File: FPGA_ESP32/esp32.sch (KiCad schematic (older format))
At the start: 1 part

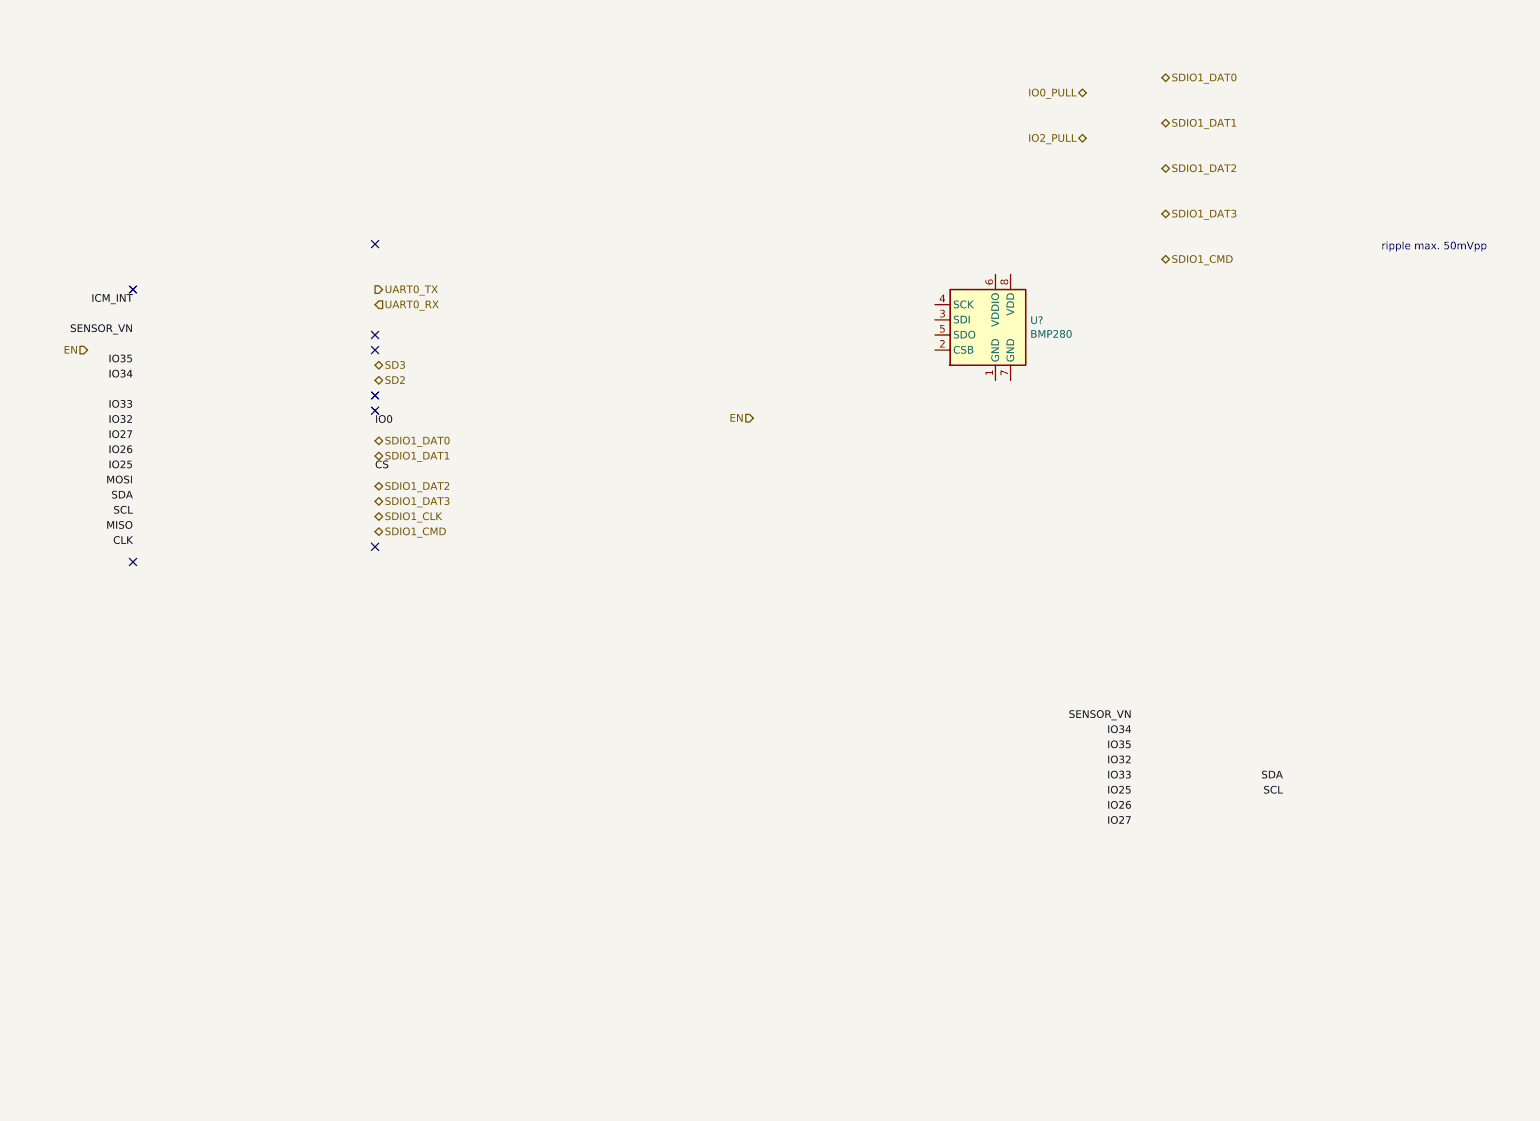
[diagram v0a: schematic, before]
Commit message: FPGA_ESP32 : add header + esp32 with SDIO
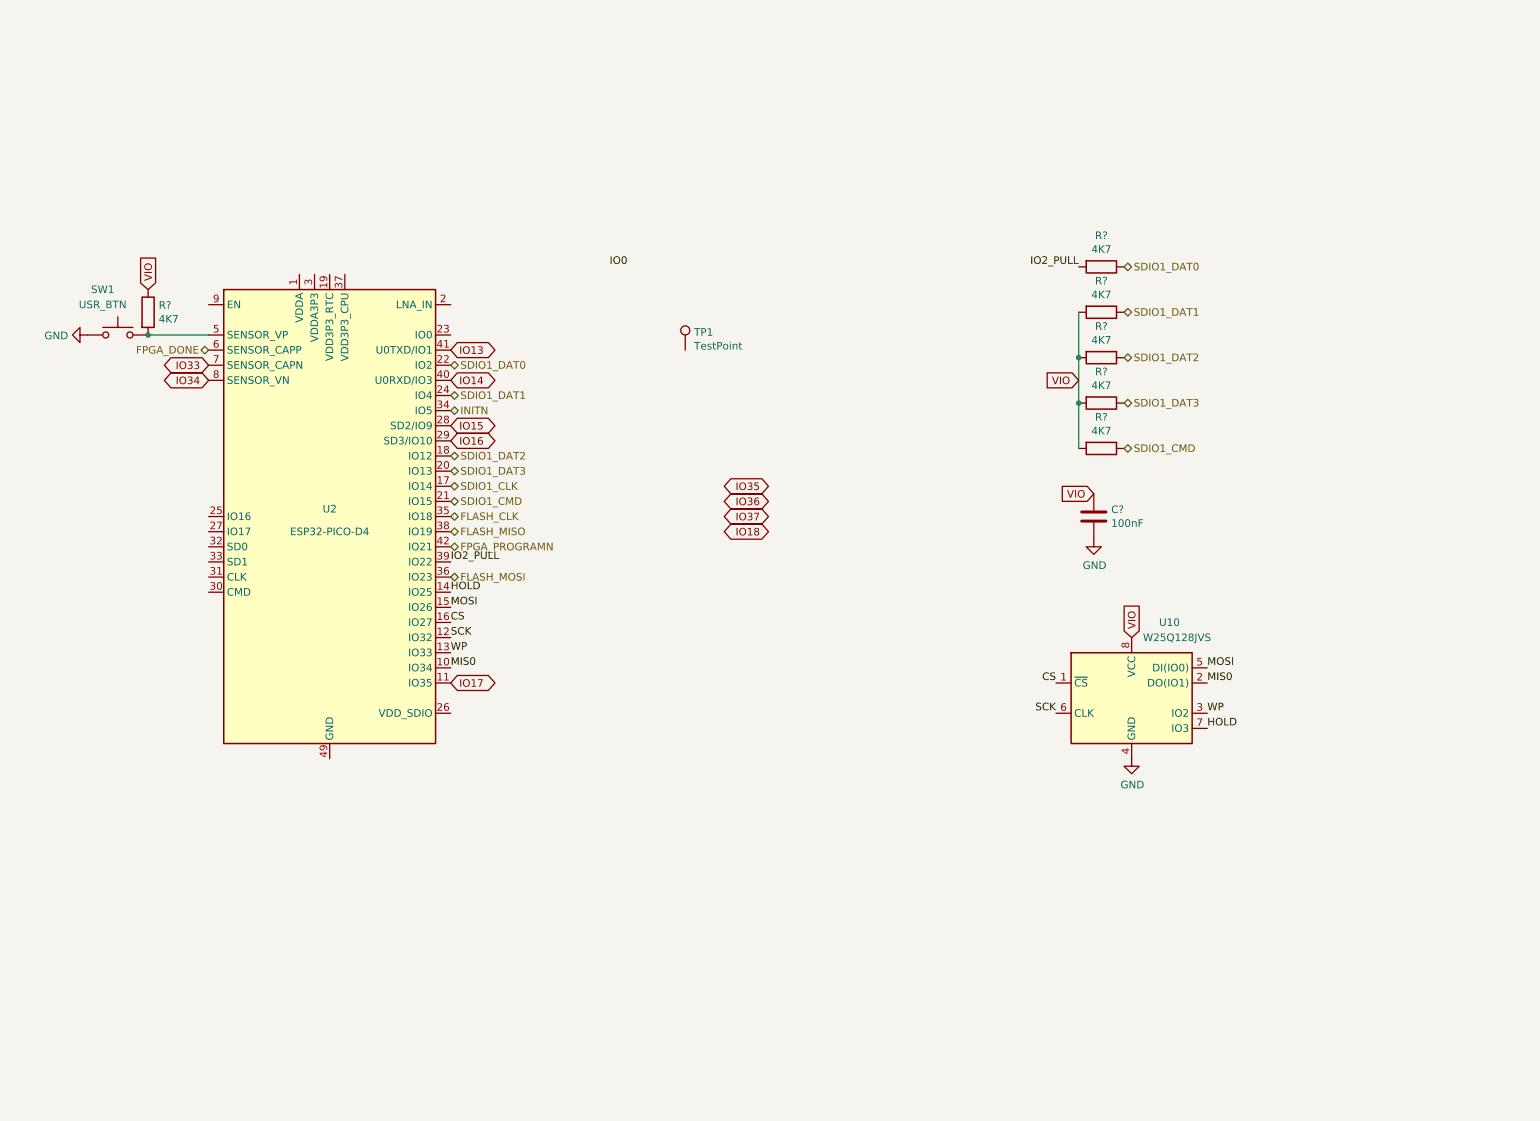
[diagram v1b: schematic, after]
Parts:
- removed U?: BMP280, Package_LGA:Bosch_LGA-8_2x2.5mm_P0.65mm_ClockwisePinNumbering, symbol Sensor_Pressure:BMP280
- added C?: 100nF, symbol Device:C
- added R? (x6): 4K7, symbol Device:R
- added SW1: USR_BTN, Button_Switch_SMD:SW_Push_1P1T_NO_CK_KMR2, symbol Switch:SW_Push
- added TP1: TestPoint, Connector_PinHeader_2.54mm:PinHeader_1x01_P2.54mm_Vertical, symbol Connector:TestPoint
- added U10: W25Q128JVS, Package_SO:SOIC-8_5.23x5.23mm_P1.27mm, symbol Memory_Flash:W25Q128JVS
- added U2: ESP32-PICO-D4, Package_DFN_QFN:QFN-48-1EP_7x7mm_P0.5mm_EP5.3x5.3mm, symbol RF_Module:ESP32-PICO-D4
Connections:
- net CS: now also U10.1 (~CS), U2.16 (IO27)
- net IO2_PULL: now also R?.2, U2.39 (IO22)
- net IO33: now also U2.7 (SENSOR_CAPN)
- net IO34: now also U2.8 (SENSOR_VN)
- net MOSI: now also U10.5 (DI(IO0)), U2.15 (IO26)
- net SDIO1_CLK: now also U2.17 (IO14)
- net SDIO1_CMD: now also R?.1, U2.21 (IO15)
- net SDIO1_DAT0: now also R?.1, U2.22 (IO2)
- net SDIO1_DAT1: now also R?.1, U2.24 (IO4)
- net SDIO1_DAT2: now also R?.1, U2.18 (IO12)
- net SDIO1_DAT3: now also R?.1, U2.20 (IO13)
- new net: R?.2, SW1.2, U2.5 (SENSOR_VP)
- new net: U2.1 (VDDA), U2.43 (VDDA), U2.46 (VDDA)
- new net: U2.3 (VDDA3P3), U2.4 (VDDA3P3)
- new net FLASH_CLK: U2.35 (IO18)
- new net FLASH_MISO: U2.38 (IO19)
- new net FLASH_MOSI: U2.36 (IO23)
- new net FPGA_DONE: U2.6 (SENSOR_CAPP)
- new net FPGA_PROGRAMN: U2.42 (IO21)
- new net GND: C?.1, SW1.1, U10.4 (GND)
- new net HOLD: U10.7 (IO3), U2.14 (IO25)
- new net INITN: U2.34 (IO5)
- new net IO13: U2.41 (U0TXD/IO1)
- new net IO14: U2.40 (U0RXD/IO3)
- new net IO15: U2.28 (SD2/IO9)
- new net IO16: U2.29 (SD3/IO10)
- new net IO17: U2.11 (IO35)
- new net MIS0: U10.2 (DO(IO1)), U2.10 (IO34)
- new net SCK: U10.6 (CLK), U2.12 (IO32)
- new net VIO: C?.2, R?.1, R?.2, R?.2, R?.2, R?.2, U10.8 (VCC)
- new net WP: U10.3 (IO2), U2.13 (IO33)
- no-connect marks 8 -> 0
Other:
- note removed: "ripple max. 50mVpp"

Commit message: FPGA_ESP32 : add 2 psram ic, rf switch
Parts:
- removed R?: 4K7, symbol Device:R
- removed SW1: USR_BTN, Button_Switch_SMD:SW_Push_1P1T_NO_CK_KMR2, symbol Switch:SW_Push
- removed U10: W25Q128JVS, Package_SO:SOIC-8_5.23x5.23mm_P1.27mm, symbol Memory_Flash:W25Q128JVS
- added ANT2: Antenna, TestPoint:TestPoint_Pad_D1.0mm, symbol Connector:TestPoint
- added U10: GD25Q16CEIGR, footprints:PSON50P200X300X50-9N, symbol GD25Q16CEIGR:GD25Q16CEIGR
- added U7: RFX2411, footprints:QFN-20_EP_3x3_Pitch0.4mm, symbol ob:RFX2411
- ANT1: renamed from TP1; value TestPoint -> Antenna; footprint Connector_PinHeader_2.54mm:PinHeader_1x01_P2.54mm_Vertical -> TestPoint:TestPoint_Pad_D1.0mm
- C6: renamed from C?; footprint (none) -> Capacitor_SMD:C_0402_1005Metric
- R10, R11, R7, R8, R9: renamed from R?; footprint (none) -> Resistor_SMD:R_0201_0603Metric
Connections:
- net labels removed: IO0, IO36, IO37, MIS0, MOSI, SCK
- wire segments 4 -> 3
- no-connect marks 0 -> 6
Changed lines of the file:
@@
 Text HLabel 8400 3050 2    50   BiDi ~ 0
 SDIO1_DAT3
-Text Label 5000 2150 0    50   ~ 0
-IO0
 $Comp
 L RF_Module:ESP32-PICO-D4 U2
@@
 $EndComp
 $Comp
-L Connector:TestPoint TP1
+L Connector:TestPoint ANT1
 U 1 1 5F0A52BA
 P 5500 2700
-F 0 "TP1" H 5558 2818 50  0000 L CNN
-F 1 "TestPoint" H 5558 2727 50  0000 L CNN
-F 2 "Connector_PinHeader_2.54mm:PinHeader_1x01_P2.54mm_Vertical" H 5700 2700 50  0001 C CNN
+F 0 "ANT1" H 5558 2818 50  0000 L CNN
+F 1 "Antenna" H 5558 2727 50  0000 L CNN
+F 2 "TestPoint:TestPoint_Pad_D1.0mm" H 5700 2700 50  0001 C CNN
 F 3 "~" H 5700 2700 50  0001 C CNN
 	1    5500 2700
-	1    0    0    -1
-$EndComp
-$Comp
-L Switch:SW_Push SW1
-U 1 1 5EFD2740
-P 1750 2600
-F 0 "SW1" H 1650 2900 50  0000 C CNN
-F 1 "USR_BTN" H 1650 2800 50  0000 C CNN
-F 2 "Button_Switch_SMD:SW_Push_1P1T_NO_CK_KMR2" H 1750 2800 50  0001 C CNN
-F 3 "~" H 1750 2800 50  0001 C CNN
-	1    1750 2600
-	1    0    0    -1
-$EndComp
-$Comp
-L Memory_Flash:W25Q128JVS U10
-U 1 1 5F0603B1
-P 8450 5000
-F 0 "U10" H 8700 5500 50  0000 C CNN
-F 1 "W25Q128JVS" H 8750 5400 50  0000 C CNN
-F 2 "Package_SO:SOIC-8_5.23x5.23mm_P1.27mm" H 8450 5000 50  0001 C CNN
-F 3 "http://www.winbond.com/resource-files/w25q128jv_dtr%20revc%2003272018%20plus.pdf" H 8450 5000 50  0001 C CNN
-	1    8450 5000
 	1    0    0    -1
 $EndComp
@@
 Text GLabel 3950 4900 2    50   BiDi ~ 0
 IO17
-Text GLabel 6050 3900 0    50   BiDi ~ 0
+Text GLabel 2350 2600 0    50   BiDi ~ 0
 IO18
 Text GLabel 2350 2800 0    50   BiDi ~ 0
@@
 Text GLabel 2350 2900 0    50   BiDi ~ 0
 IO34
-Text GLabel 6050 3600 0    50   BiDi ~ 0
+Text GLabel 3950 2600 2    50   BiDi ~ 0
 IO35
-Text GLabel 6050 3700 0    50   BiDi ~ 0
-IO36
-Text GLabel 6050 3800 0    50   BiDi ~ 0
-IO37
 Text HLabel 2350 2700 0    50   BiDi ~ 0
 FPGA_DONE
@@
 FLASH_CLK
 $Comp
-L Device:R R?
+L Device:R R7
 U 1 1 5F21A72D
 P 8250 2150
-F 0 "R?" V 8043 2150 50  0000 C CNN
+F 0 "R7" V 8043 2150 50  0000 C CNN
 F 1 "4K7" V 8134 2150 50  0000 C CNN
-F 2 "" V 8180 2150 50  0001 C CNN
+F 2 "Resistor_SMD:R_0201_0603Metric" V 8180 2150 50  0001 C CNN
 F 3 "~" H 8250 2150 50  0001 C CNN
 	1    8250 2150
@@
 $EndComp
 $Comp
-L Device:R R?
+L Device:R R8
 U 1 1 5F21B20B
 P 8250 2450
-F 0 "R?" V 8043 2450 50  0000 C CNN
+F 0 "R8" V 8043 2450 50  0000 C CNN
 F 1 "4K7" V 8134 2450 50  0000 C CNN
-F 2 "" V 8180 2450 50  0001 C CNN
+F 2 "Resistor_SMD:R_0201_0603Metric" V 8180 2450 50  0001 C CNN
 F 3 "~" H 8250 2450 50  0001 C CNN
 	1    8250 2450
@@
 $EndComp
 $Comp
-L Device:R R?
+L Device:R R9
 U 1 1 5F21B520
 P 8250 2750
-F 0 "R?" V 8043 2750 50  0000 C CNN
+F 0 "R9" V 8043 2750 50  0000 C CNN
 F 1 "4K7" V 8134 2750 50  0000 C CNN
-F 2 "" V 8180 2750 50  0001 C CNN
+F 2 "Resistor_SMD:R_0201_0603Metric" V 8180 2750 50  0001 C CNN
 F 3 "~" H 8250 2750 50  0001 C CNN
 	1    8250 2750
@@
 $EndComp
 $Comp
-L Device:R R?
+L Device:R R10
 U 1 1 5F21B89E
 P 8250 3050
-F 0 "R?" V 8043 3050 50  0000 C CNN
+F 0 "R10" V 8043 3050 50  0000 C CNN
 F 1 "4K7" V 8134 3050 50  0000 C CNN
-F 2 "" V 8180 3050 50  0001 C CNN
+F 2 "Resistor_SMD:R_0201_0603Metric" V 8180 3050 50  0001 C CNN
 F 3 "~" H 8250 3050 50  0001 C CNN
 	1    8250 3050
@@
 $EndComp
 $Comp
-L Device:R R?
+L Device:R R11
 U 1 1 5F21BAF6
 P 8250 3350
-F 0 "R?" V 8043 3350 50  0000 C CNN
+F 0 "R11" V 8043 3350 50  0000 C CNN
 F 1 "4K7" V 8134 3350 50  0000 C CNN
-F 2 "" V 8180 3350 50  0001 C CNN
+F 2 "Resistor_SMD:R_0201_0603Metric" V 8180 3350 50  0001 C CNN
 F 3 "~" H 8250 3350 50  0001 C CNN
 	1    8250 3350
@@
 IO2_PULL
 $Comp
-L power:GND #PWR?
+L power:GND #PWR0120
 U 1 1 5F221A50
-P 8450 5400
-F 0 "#PWR?" H 8450 5150 50  0001 C CNN
-F 1 "GND" H 8455 5227 50  0000 C CNN
-F 2 "" H 8450 5400 50  0001 C CNN
-F 3 "" H 8450 5400 50  0001 C CNN
-	1    8450 5400
-	1    0    0    -1
-$EndComp
-$Comp
-L power:GND #PWR?
-U 1 1 5F2233EE
-P 1550 2600
-F 0 "#PWR?" H 1550 2350 50  0001 C CNN
-F 1 "GND" V 1555 2472 50  0000 R CNN
-F 2 "" H 1550 2600 50  0001 C CNN
-F 3 "" H 1550 2600 50  0001 C CNN
-	1    1550 2600
-	0    1    1    0
-$EndComp
-$Comp
-L Device:R R?
-U 1 1 5F22533D
-P 1950 2450
-F 0 "R?" H 2020 2496 50  0000 L CNN
-F 1 "4K7" H 2020 2405 50  0000 L CNN
-F 2 "" V 1880 2450 50  0001 C CNN
-F 3 "~" H 1950 2450 50  0001 C CNN
-	1    1950 2450
-	1    0    0    -1
-$EndComp
-Wire Wire Line
-	1950 2600 2350 2600
-Connection ~ 1950 2600
-Text GLabel 1950 2300 1    50   Input ~ 0
-VIO
-Text Label 3950 4400 0    50   ~ 0
-MOSI
-Text Label 3950 4800 0    50   ~ 0
-MIS0
-Text Label 3950 4600 0    50   ~ 0
-SCK
-Text Label 3950 4700 0    50   ~ 0
+P 9250 5800
+F 0 "#PWR0120" H 9250 5550 50  0001 C CNN
+F 1 "GND" H 9255 5627 50  0000 C CNN
+F 2 "" H 9250 5800 50  0001 C CNN
+F 3 "" H 9250 5800 50  0001 C CNN
+	1    9250 5800
+	0    -1   -1   0
+$EndComp
+Text Label 3950 4500 0    50   ~ 0
 WP
 Text Label 3950 4300 0    50   ~ 0
 HOLD
-Text Label 8950 4800 0    50   ~ 0
-MOSI
-Text Label 8950 4900 0    50   ~ 0
-MIS0
-Text Label 7950 5100 2    50   ~ 0
-SCK
-Text Label 8950 5100 0    50   ~ 0
+Text Label 9250 5400 0    50   ~ 0
 WP
-Text Label 8950 5200 0    50   ~ 0
+Text Label 9250 5500 0    50   ~ 0
 HOLD
-Text Label 3950 4500 0    50   ~ 0
+Text Label 3950 4400 0    50   ~ 0
 CS
-Text Label 7950 4900 2    50   ~ 0
+Text Label 7650 5200 2    50   ~ 0
 CS
 $Comp
-L Device:C C?
+L Device:C C6
 U 1 1 5F22BD65
 P 8200 3800
-F 0 "C?" H 8085 3754 50  0000 R CNN
+F 0 "C6" H 8085 3754 50  0000 R CNN
 F 1 "100nF" H 8085 3845 50  0000 R CNN
-F 2 "" H 8238 3650 50  0001 C CNN
+F 2 "Capacitor_SMD:C_0402_1005Metric" H 8238 3650 50  0001 C CNN
 F 3 "~" H 8200 3800 50  0001 C CNN
 	1    8200 3800
@@
 VIO
 $Comp
-L power:GND #PWR?
+L power:GND #PWR0122
 U 1 1 5F22D916
 P 8200 3950
-F 0 "#PWR?" H 8200 3700 50  0001 C CNN
+F 0 "#PWR0122" H 8200 3700 50  0001 C CNN
 F 1 "GND" H 8205 3777 50  0000 C CNN
 F 2 "" H 8200 3950 50  0001 C CNN
@@
 	1    0    0    -1
 $EndComp
-Text GLabel 8450 4600 1    50   Input ~ 0
+Text GLabel 9250 5100 2    50   Input ~ 0
 VIO
+NoConn ~ 2350 3800
+NoConn ~ 2350 3900
+NoConn ~ 2350 4000
+NoConn ~ 2350 4100
+NoConn ~ 2350 4200
+NoConn ~ 2350 4300
+$Comp
+L power:GND #PWR0123
+U 1 1 5F242AB9
+P 3150 5400
+F 0 "#PWR0123" H 3150 5150 50  0001 C CNN
+F 1 "GND" H 3155 5227 50  0000 C CNN
+F 2 "" H 3150 5400 50  0001 C CNN
+F 3 "" H 3150 5400 50  0001 C CNN
+	1    3150 5400
+	1    0    0    -1
+$EndComp
+Text HLabel 7650 5600 0    50   BiDi ~ 0
+FLASH_MISO
+Text HLabel 7650 5300 0    50   BiDi ~ 0
+FLASH_CLK
+Text HLabel 7650 5500 0    50   BiDi ~ 0
+FLASH_MOSI
+$Comp
+L GD25Q16CEIGR:GD25Q16CEIGR U10
+U 1 1 5EE69D48
+P 8450 5400
+F 0 "U10" H 8450 5967 50  0000 C CNN
+F 1 "GD25Q16CEIGR" H 8450 5876 50  0000 C CNN
+F 2 "footprints:PSON50P200X300X50-9N" H 8450 5400 50  0001 L BNN
+F 3 "3.0" H 8450 5400 50  0001 L BNN
+F 4 "GigaDevice" H 8450 5400 50  0001 L BNN "Field4"
+F 5 "IPC 7351B" H 8450 5400 50  0001 L BNN "Field5"
+F 6 "0.5 mm" H 8450 5400 50  0001 L BNN "Field6"
+	1    8450 5400
+	1    0    0    -1
+$EndComp
+$Comp
+L Connector:TestPoint ANT2
+U 1 1 5EF38F43
+P 5500 2950
+F 0 "ANT2" H 5558 3068 50  0000 L CNN
+F 1 "Antenna" H 5558 2977 50  0000 L CNN
+F 2 "TestPoint:TestPoint_Pad_D1.0mm" H 5700 2950 50  0001 C CNN
+F 3 "~" H 5700 2950 50  0001 C CNN
+	1    5500 2950
+	1    0    0    -1
+$EndComp
+$Comp
+L ob:RFX2411 U7
+U 1 1 5EF3C8E7
+P 6050 4500
+F 0 "U7" H 6050 5731 50  0000 C CNN
+F 1 "RFX2411" H 6050 5640 50  0000 C CNN
+F 2 "footprints:QFN-20_EP_3x3_Pitch0.4mm" H 6050 4750 50  0001 C CNN
+F 3 "" H 6050 4750 50  0001 C CNN
+	1    6050 4500
+	1    0    0    -1
+$EndComp
 $EndSCHEMATC

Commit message: FPGA_ESP32 : add spi mux
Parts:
- added U3: TMUX1574, footprints:QFP-16_1.85x2.65_Pitch0.4mm, symbol ob:TMUX1574
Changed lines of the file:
@@
 L power:GND #PWR0120
 U 1 1 5F221A50
-P 9250 5800
-F 0 "#PWR0120" H 9250 5550 50  0001 C CNN
-F 1 "GND" H 9255 5627 50  0000 C CNN
-F 2 "" H 9250 5800 50  0001 C CNN
-F 3 "" H 9250 5800 50  0001 C CNN
-	1    9250 5800
+P 10550 5750
+F 0 "#PWR0120" H 10550 5500 50  0001 C CNN
+F 1 "GND" H 10555 5577 50  0000 C CNN
+F 2 "" H 10550 5750 50  0001 C CNN
+F 3 "" H 10550 5750 50  0001 C CNN
+	1    10550 5750
 	0    -1   -1   0
 $EndComp
@@
 Text Label 3950 4300 0    50   ~ 0
 HOLD
-Text Label 9250 5400 0    50   ~ 0
+Text Label 10550 5350 0    50   ~ 0
 WP
-Text Label 9250 5500 0    50   ~ 0
+Text Label 10550 5450 0    50   ~ 0
 HOLD
 Text Label 3950 4400 0    50   ~ 0
 CS
-Text Label 7650 5200 2    50   ~ 0
+Text Label 8950 5150 2    50   ~ 0
 CS
 $Comp
@@
 	1    0    0    -1
 $EndComp
-Text GLabel 9250 5100 2    50   Input ~ 0
+Text GLabel 10550 5050 2    50   Input ~ 0
 VIO
 NoConn ~ 2350 3800
@@
 	1    0    0    -1
 $EndComp
-Text HLabel 7650 5600 0    50   BiDi ~ 0
+Text HLabel 8950 5550 0    50   BiDi ~ 0
 FLASH_MISO
-Text HLabel 7650 5300 0    50   BiDi ~ 0
+Text HLabel 8950 5250 0    50   BiDi ~ 0
 FLASH_CLK
-Text HLabel 7650 5500 0    50   BiDi ~ 0
+Text HLabel 8950 5450 0    50   BiDi ~ 0
 FLASH_MOSI
 $Comp
 L GD25Q16CEIGR:GD25Q16CEIGR U10
 U 1 1 5EE69D48
-P 8450 5400
-F 0 "U10" H 8450 5967 50  0000 C CNN
-F 1 "GD25Q16CEIGR" H 8450 5876 50  0000 C CNN
-F 2 "footprints:PSON50P200X300X50-9N" H 8450 5400 50  0001 L BNN
-F 3 "3.0" H 8450 5400 50  0001 L BNN
-F 4 "GigaDevice" H 8450 5400 50  0001 L BNN "Field4"
-F 5 "IPC 7351B" H 8450 5400 50  0001 L BNN "Field5"
-F 6 "0.5 mm" H 8450 5400 50  0001 L BNN "Field6"
-	1    8450 5400
+P 9750 5350
+F 0 "U10" H 9750 5917 50  0000 C CNN
+F 1 "GD25Q16CEIGR" H 9750 5826 50  0000 C CNN
+F 2 "footprints:PSON50P200X300X50-9N" H 9750 5350 50  0001 L BNN
+F 3 "3.0" H 9750 5350 50  0001 L BNN
+F 4 "GigaDevice" H 9750 5350 50  0001 L BNN "Field4"
+F 5 "IPC 7351B" H 9750 5350 50  0001 L BNN "Field5"
+F 6 "0.5 mm" H 9750 5350 50  0001 L BNN "Field6"
+	1    9750 5350
 	1    0    0    -1
 $EndComp
@@
 	1    0    0    -1
 $EndComp
+$Comp
+L ob:TMUX1574 U3
+U 1 1 5EF70941
+P 7700 5400
+F 0 "U3" H 7675 6231 50  0000 C CNN
+F 1 "TMUX1574" H 7675 6140 50  0000 C CNN
+F 2 "footprints:QFP-16_1.85x2.65_Pitch0.4mm" H 7700 5400 50  0001 C CNN
+F 3 "" H 7700 5400 50  0001 C CNN
+	1    7700 5400
+	1    0    0    -1
+$EndComp

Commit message: FPGA_ESP32 : add camera, change header position
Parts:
- added C10: 1uF, Capacitor_SMD:C_0402_1005Metric, symbol Device:C
- added C11, C8, C9: 0.1uF, Capacitor_SMD:C_0402_1005Metric, symbol Device:C
- added C12, C13: C, Capacitor_SMD:C_0402_1005Metric, symbol Device:C
- added C2, C3: 220pF, Capacitor_SMD:C_0402_1005Metric, symbol Device:C
- added C4, C5: 2.2uF, Capacitor_SMD:C_0402_1005Metric, symbol Device:C
- added L1: 1.2nH, Inductor_SMD:L_0402_1005Metric, symbol Device:L
- added L2: L, symbol Device:L
- added R16, R17, R18, R19: 1K, Resistor_SMD:R_0201_0603Metric, symbol Device:R
- added R6: 10K, Resistor_SMD:R_0201_0603Metric, symbol Device:R
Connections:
- net labels added: CLK, EN, FLASH_HOLD, IO40, MISO, MODE, MOSI, PDET, RXEN, SEL, SPI_EN, SWANT, TXEN, TXRX
- net labels removed: IO15, IO16, IO34
- wire segments 3 -> 39
- no-connect marks 6 -> 7
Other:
- moved on the sheet: ANT1, ANT2, C6, R10, R11, R7, R8, R9, U2

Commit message: FPGA_ESP32 : lot of fix + modification
Replace digital camera by analog camera decoder
Fix PSRAM io domain 3.3V -> 1.8V
Start reducing capacitor number
Add remaining psram pin
Sheet resize
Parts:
- removed C5: 2.2uF, Capacitor_SMD:C_0402_1005Metric, symbol Device:C
- L2: footprint (none) -> Inductor_SMD:L_0402_1005Metric
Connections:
- wire segments 39 -> 37
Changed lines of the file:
@@
 	-1   0    0    1
 $EndComp
-$Comp
-L Device:C C5
-U 1 1 5F0D4062
-P 10600 950
-F 0 "C5" H 10850 900 50  0000 C CNN
-F 1 "2.2uF" H 10850 1000 50  0000 C CNN
-F 2 "Capacitor_SMD:C_0402_1005Metric" H 10638 800 50  0001 C CNN
-F 3 "~" H 10600 950 50  0001 C CNN
-	1    10600 950
-	-1   0    0    1
-$EndComp
-Wire Wire Line
-	10600 1100 10100 1100
 Connection ~ 9600 1100
 Wire Wire Line
 	9600 1100 9100 1100
-Connection ~ 10100 1100
 Wire Wire Line
 	10100 1100 9600 1100
@@
 Wire Wire Line
 	9600 800  10100 800
-Connection ~ 10100 800
-Wire Wire Line
-	10100 800  10600 800
 Text GLabel 9700 1350 0    50   Input ~ 0
 VIO
@@
 F 0 "L2" H 4103 1896 50  0000 L CNN
 F 1 "L" H 4103 1805 50  0000 L CNN
-F 2 "" H 4050 1850 50  0001 C CNN
+F 2 "Inductor_SMD:L_0402_1005Metric" H 4050 1850 50  0001 C CNN
 F 3 "~" H 4050 1850 50  0001 C CNN
 	1    4050 1850

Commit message: FPGA_ESP32 : esp32 enable circuit, flash done, more doc, TODO power !
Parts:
- added C?: 0.1uF, Capacitor_SMD:C_0402_1005Metric, symbol Device:C
- added R?: 10K, symbol Device:R
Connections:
- net labels added: IO27
- net labels removed: FPGA_DONE, INITN, IO33, SPI_EN
- wire segments 37 -> 39
- no-connect marks 7 -> 8
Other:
- moved on the sheet: ANT1, ANT2, C10, C12, C13, C2, C3, C4, C6, C8, C9, L1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
